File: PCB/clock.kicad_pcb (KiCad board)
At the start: 2 copper layers, 202.1 x 84.3 mm, 31 parts, among them J1 USB_C_Receptacle, J2 Conn_01x08, J3 Conn_01x02_Pin, J4 Conn_01x05, J5 Conn_01x05, J6 Conn_01x08, J7 Conn_01x02_Pin, J8 Conn_01x05, J9 Conn_01x05, SW1 RotaryEncoder_Switch_MP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

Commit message: Add files via upload
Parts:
- removed D3: D, Diode_SMD:D_0603_1608Metric_Pad1.05x0.95mm_HandSolder
- removed J7: Conn_01x02_Pin, Connector_JST:JST_XH_B2B-XH-A_1x02_P2.50mm_Vertical
- removed J9: Conn_01x05, Connector_JST:JST_XH_B5B-XH-A_1x05_P2.50mm_Vertical
- removed the REF** at (157.5, 122.5)
- removed the REF** at (191.0, 122.5)
- removed the REF** at (217.2, 90.0)
- removed the REF** at (157.5, 147.0)
- removed SW2: RotaryEncoder_Switch_MP, ScottoKeebs_Scotto:Encoder_EC11_MX
- added BZ1: Buzzer, Buzzer_Beeper:Buzzer_12x9.5RM7.6, B.Cu at (89.7, 177.5)
- added BZ2: Buzzer, Buzzer_Beeper:Buzzer_12x9.5RM7.6, B.Cu at (121.7, 177.5)
- added Q1: 2N3904, Package_TO_SOT_THT:TO-92_HandSolder, B.Cu at (121.0, 168.5)
- added Q2: 2N3904, Package_TO_SOT_THT:TO-92_HandSolder, B.Cu at (128.0, 168.5)
- added R4: 1kΩ, Capacitor_SMD:C_0603_1608Metric_Pad1.08x0.95mm_HandSolder, F.Cu at (145.5, 171.1)
- added R5: 1kΩ, Capacitor_SMD:C_0603_1608Metric_Pad1.08x0.95mm_HandSolder, F.Cu at (145.5, 175.5)
- J3: value Conn_01x02_Pin -> Conn_01x05; footprint Connector_JST:JST_XH_B2B-XH-A_1x02_P2.50mm_Vertical -> Connector_JST:JST_XH_B5B-XH-A_1x05_P2.50mm_Vertical
- J5: moved to F.Cu
- moved D1 136.3 mm to (109.4, 182.5)
- moved REF** 136.3 mm to (138.2, 174.5)
- moved REF** 136.3 mm to (80.2, 174.5)
- moved S1 136.3 mm to (109.4, 173.5)
- moved J3 131.8 mm to (97.0, 167.0), turned to 180 degrees
- moved J5 55.3 mm to (109.0, 108.0), turned to 0 degrees
- moved REF** 9.18 mm to (186.5, 139.0)
- moved J8 1.50 mm to (90.5, 108.0)
- moved J4 0.95 mm to (164.5, 142.0)
- moved J2 0.22 mm to (77.1, 136.2)
- moved LCD1 0.22 mm to (84.4, 144.9)
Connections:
- J3 pad 1: S0 -> GND
- J3 pad 2: Row 0 -> +5V
- J5 pad 2: S2 -> +5V
- J5 pad 3: E2A -> buzzer 0
- J5 pad 4: E2B -> Row 0 O
- J5 pad 5: Row 2 -> S0 O
- U1 pad 38: unconnected-(U1-IO42-Pad38) -> buzzer 0
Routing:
- net buzzer: track 0.00 -> 70.0 mm
- net +5V: track 27.7 -> 91.6 mm
- net Net-(BZ1--): track 0.00 -> 38.1 mm
- net Net-(Q1-B): track 0.00 -> 28.9 mm, vias 0 -> 2
- net S2: track 24.6 -> 0.00 mm
- net E2A O: track 23.2 -> 0.20 mm, vias 1 -> 0
- net S2 O: track 29.6 -> 6.55 mm
- net Row 2 O: track 21.5 -> 0.00 mm, vias 1 -> 0
- net E2B O: track 21.2 -> 0.01 mm, vias 1 -> 0
- net Row 0: track 15.0 -> 35.9 mm
- net Net-(D3-A): track 20.0 -> 0.00 mm
- net Net-(Q2-B): track 0.00 -> 18.8 mm, vias 0 -> 1
- net Row 2: track 15.0 -> 0.00 mm
- net Row 0 O: track 9.38 -> 23.3 mm, vias 0 -> 1
- net buzzer 0: track 0.00 -> 12.0 mm
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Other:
- board size 202.1 x 84.3 mm -> 117 x 108.9 mm

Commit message: ready to submit?
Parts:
- removed D1, D2: D, Diode_SMD:D_0603_1608Metric_Pad1.05x0.95mm_HandSolder
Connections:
- J3 pad 4: Row 0 -> unconnected-(J3-Pin_4-Pad4)
- J5 pad 4: Row 0 O -> unconnected-(J5-Pin_4-Pad4)
- J6 pad 5: +3V3 -> LCD-RES
- J8 pad 5: Row 1 O -> unconnected-(J8-Pin_5-Pad5)
- S1 pad 2: Net-(D1-A) -> GND
- SW1 pad S2: Net-(D2-A) -> GND
- U1 pad 11: Row 2 O -> unconnected-(U1-IO7-Pad11)
- U1 pad 14: E2A O -> unconnected-(U1-IO10-Pad14)
- U1 pad 15: E2B O -> unconnected-(U1-IO11-Pad15)
- U1 pad 37: unconnected-(U1-IO41-Pad37) -> LCD-RES
- U1 pad 8: S2 O -> unconnected-(U1-IO4-Pad8)
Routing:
- net LCD-RES: track 0.00 -> 42.4 mm, vias 0 -> 3
- net Row 0: track 35.9 -> 0.00 mm
- net Net-(D2-A): track 20.7 -> 0.00 mm
- net Net-(D1-A): track 17.8 -> 0.00 mm, vias 1 -> 0
- net GND: track 98.5 -> 113.1 mm
- net Row 1: track 14.3 -> 0.00 mm
- net S2 O: track 6.55 -> 0.00 mm, vias 1 -> 0

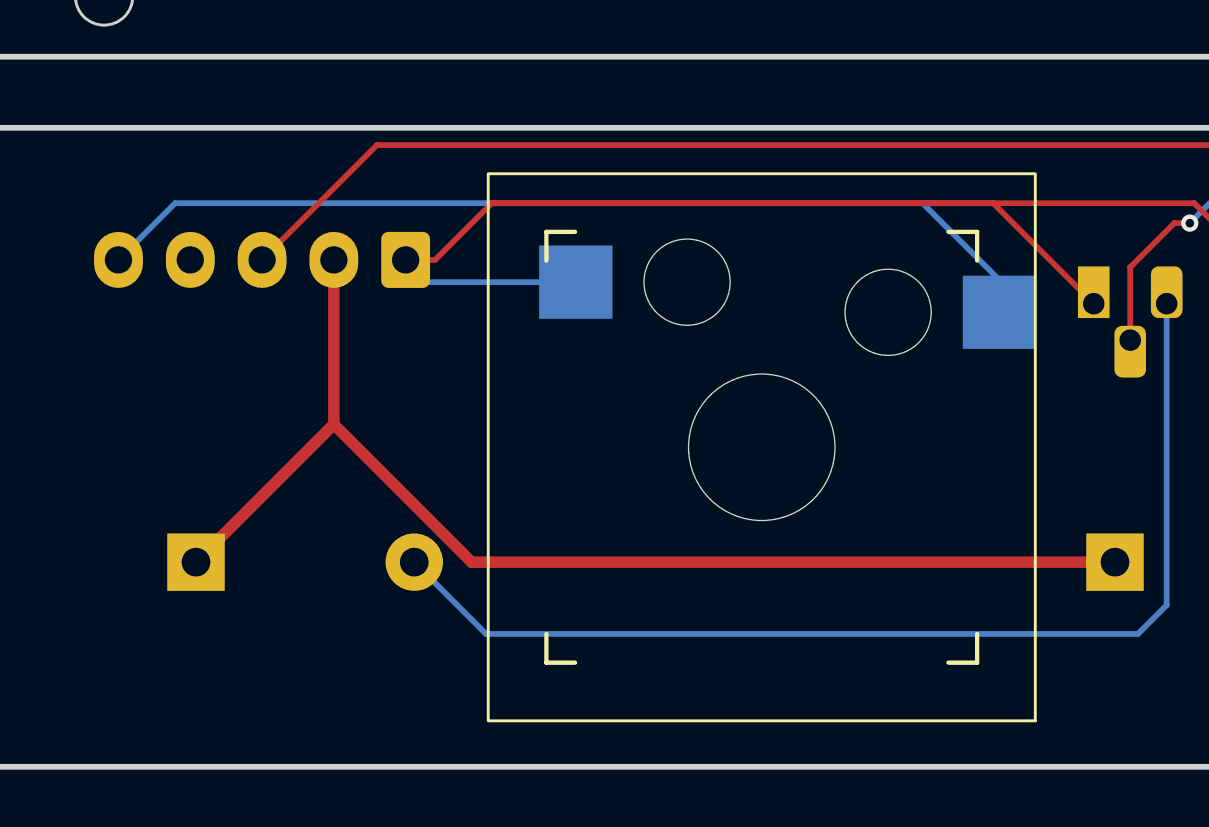
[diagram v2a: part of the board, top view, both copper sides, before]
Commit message: pcb remove hotswap switch
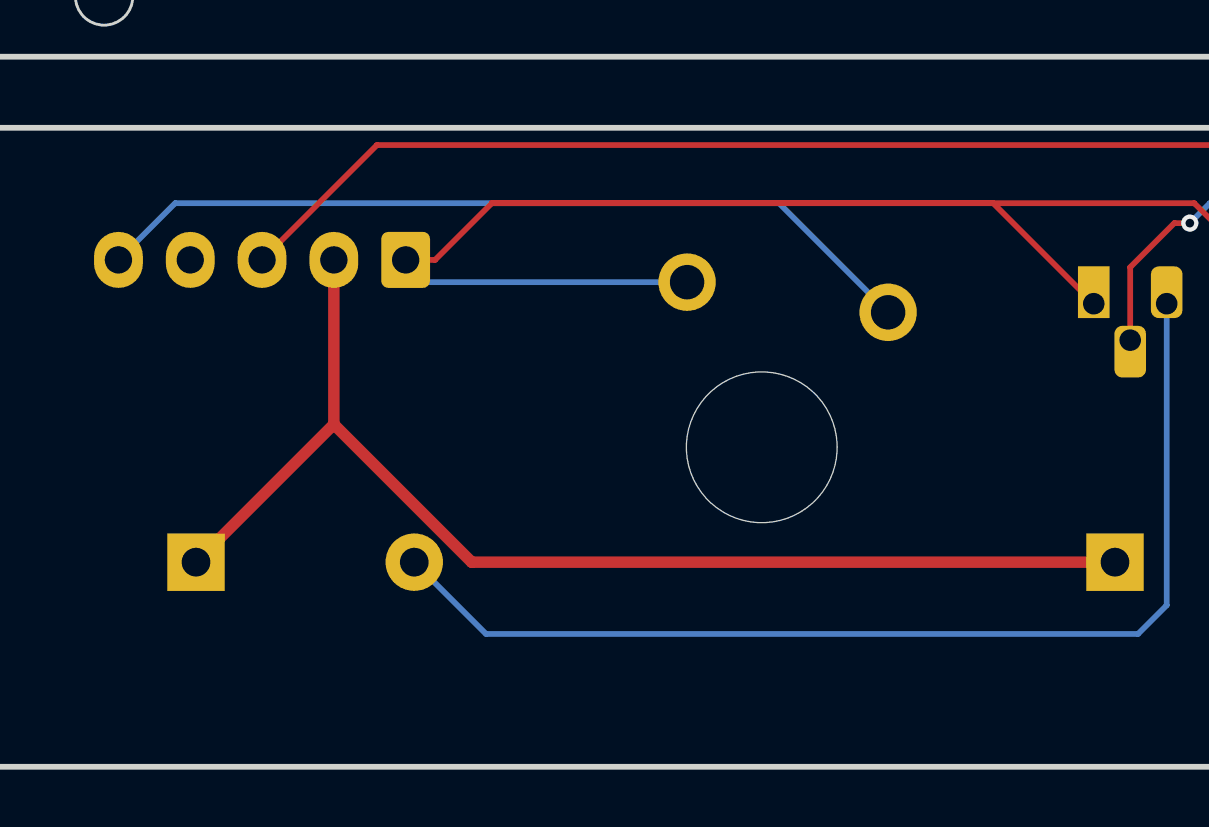
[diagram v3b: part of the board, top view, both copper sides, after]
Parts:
- S1: footprint Gateron-low-profile:Gateron_Low_Profile_Socket_1U -> marbastlib-xp-gateron_lp:SW_KS33_1u
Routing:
- net S0: track 33.7 -> 29.2 mm
- net GND: track 113.1 -> 116.9 mm

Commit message: fixes
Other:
- board text added: "1"
- board text added: "2"
- board text added: "3"
- board text added: "4"
- board text added: "built+designed by john tan-aristy"
- board text added: "ec1a"
- board text added: "https://github.com/jpt1729/Alarm-Clock"
- board text added: "jpt"
- board text added: "screen"
- board text added: "snooze"
- board text added: "sw1"

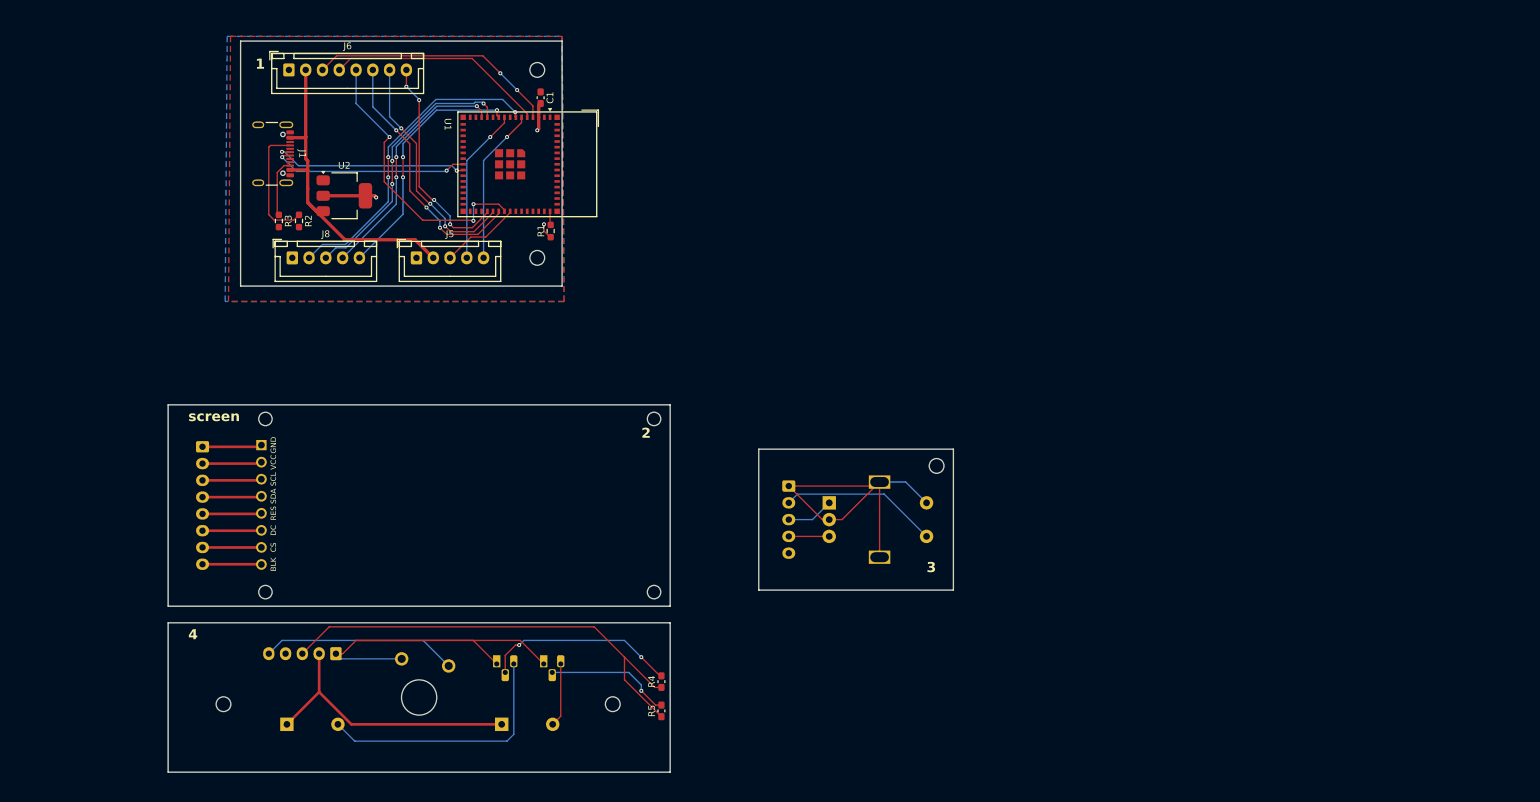
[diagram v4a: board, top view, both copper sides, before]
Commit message: pannelization
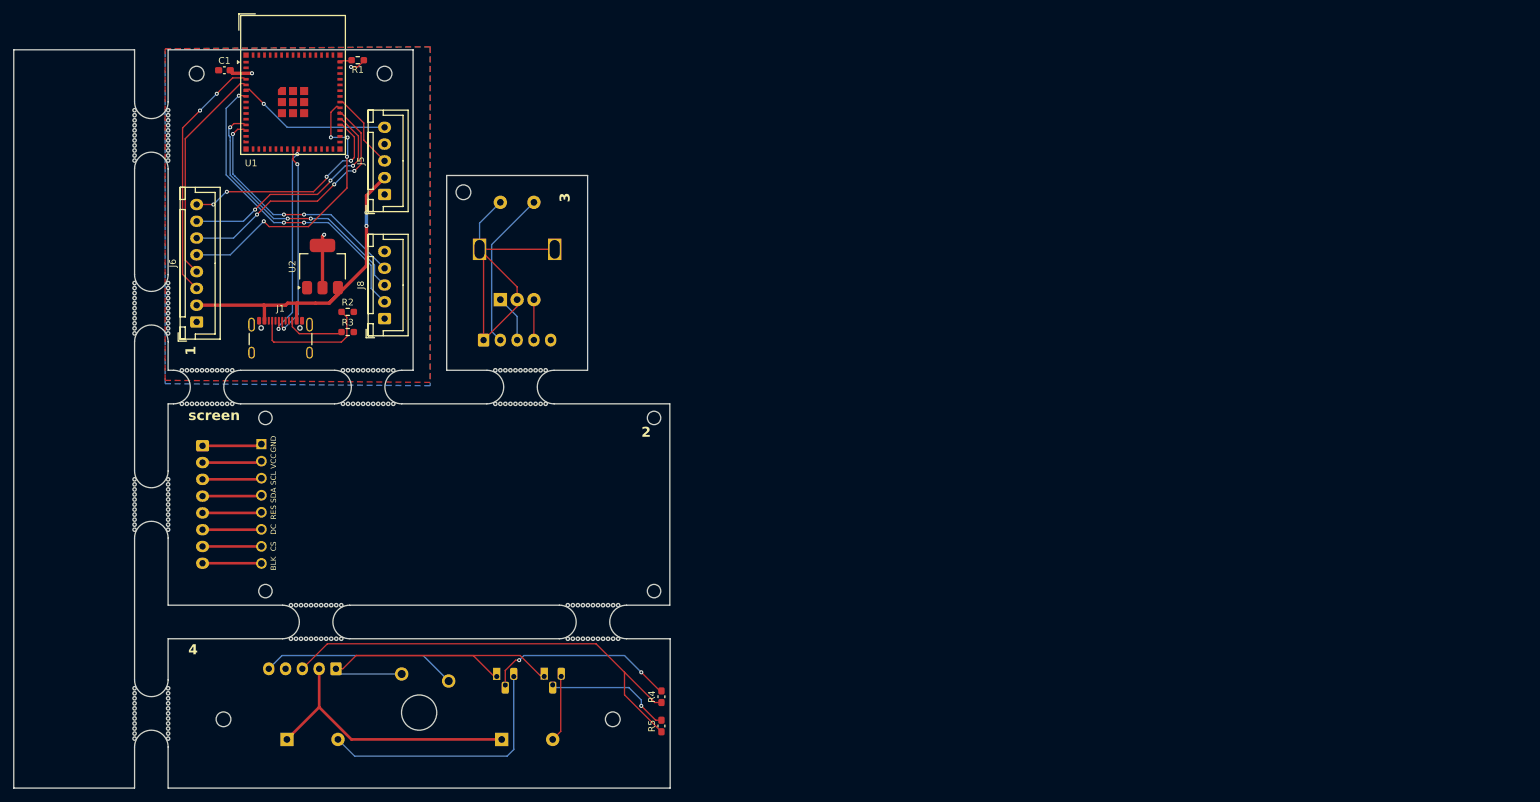
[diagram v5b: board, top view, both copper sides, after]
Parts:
- added mouse-bite-5mm-slot: VAL**, Panelization.pretty-master:mouse-bite-5mm-slot, F.Cu at (101.8, 127.2)
- added mouse-bite-5mm-slot: VAL**, Panelization.pretty-master:mouse-bite-5mm-slot, F.Cu at (94.1, 162.2)
- added mouse-bite-5mm-slot: VAL**, Panelization.pretty-master:mouse-bite-5mm-slot, F.Cu at (135.3, 162.2)
- added mouse-bite-5mm-slot: VAL**, Panelization.pretty-master:mouse-bite-5mm-slot, F.Cu at (69.5, 115.5)
- added mouse-bite-5mm-slot: VAL**, Panelization.pretty-master:mouse-bite-5mm-slot, F.Cu at (77.8, 127.2)
- added mouse-bite-5mm-slot: VAL**, Panelization.pretty-master:mouse-bite-5mm-slot, F.Cu at (69.5, 175.9)
- added mouse-bite-5mm-slot: VAL**, Panelization.pretty-master:mouse-bite-5mm-slot, F.Cu at (69.5, 144.8)
- added mouse-bite-5mm-slot: VAL**, Panelization.pretty-master:mouse-bite-5mm-slot, F.Cu at (124.5, 127.2)
- added mouse-bite-5mm-slot: VAL**, Panelization.pretty-master:mouse-bite-5mm-slot, F.Cu at (69.5, 89.8)
- moved REF** 81.4 mm to (116.0, 98.2), turned to 90 degrees
- moved SW1 67.4 mm to (124.0, 106.7), turned to 90 degrees
- moved REF** 50.8 mm to (76.2, 80.5), turned to 90 degrees
- moved J4 50.4 mm to (119.0, 120.2), turned to 0 degrees
- moved C1 47.3 mm to (80.4, 80.0), turned to 0 degrees
- moved J6 40.0 mm to (76.2, 117.5), turned to 90 degrees
- moved R1 38.4 mm to (100.2, 78.5), turned to 180 degrees
- moved U1 36.8 mm to (90.6, 82.2), turned to 0 degrees
- moved REF** 35.7 mm to (104.2, 80.5), turned to 90 degrees
- moved J1 28.6 mm to (88.8, 121.0), turned to 0 degrees
- moved R3 19.5 mm to (98.8, 119.0), turned to 0 degrees
- moved J8 16.5 mm to (104.2, 117.0), turned to 90 degrees
- moved R2 15.4 mm to (98.8, 116.0), turned to 0 degrees
- moved U2 11.0 mm to (95.0, 109.3), turned to 90 degrees
- moved J5 10.6 mm to (104.2, 98.5), turned to 90 degrees
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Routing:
- net Row 1 O: track 36.9 -> 0.00 mm, vias 3 -> 0
- net Row 0 O: track 23.3 -> 0.00 mm, vias 1 -> 0
- net +3V3: track 14.3 -> 13.5 mm
- net LCD-RES: track 42.4 -> 42.6 mm, vias 3 -> 4
- net +5V: vias 0 -> 2
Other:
- board size 117 x 108.9 mm -> 97.8 x 110 mm
